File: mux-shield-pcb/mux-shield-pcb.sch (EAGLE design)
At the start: 12 parts, among them X1 BN35N61, X2 BN35N61, X3 BU-SMB-V, X4 BU-SMB-V, X5 BU-SMA-V

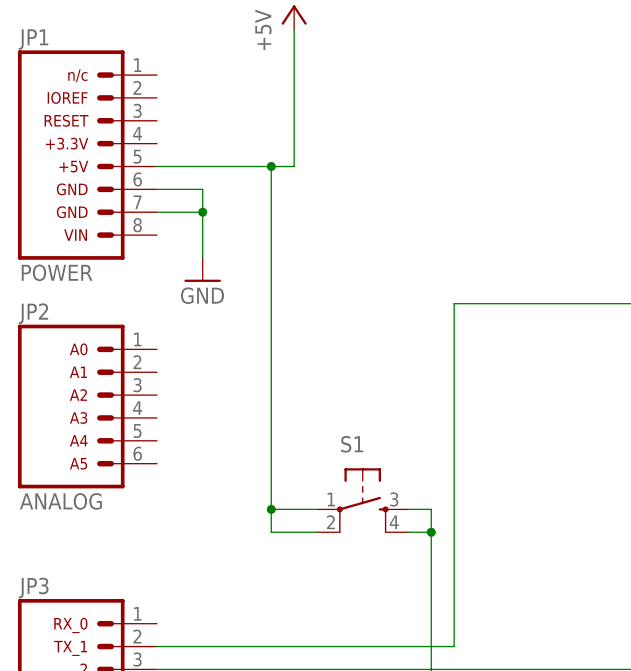
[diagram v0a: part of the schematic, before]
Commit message: Update PCB connecting button to ground rather than 5V
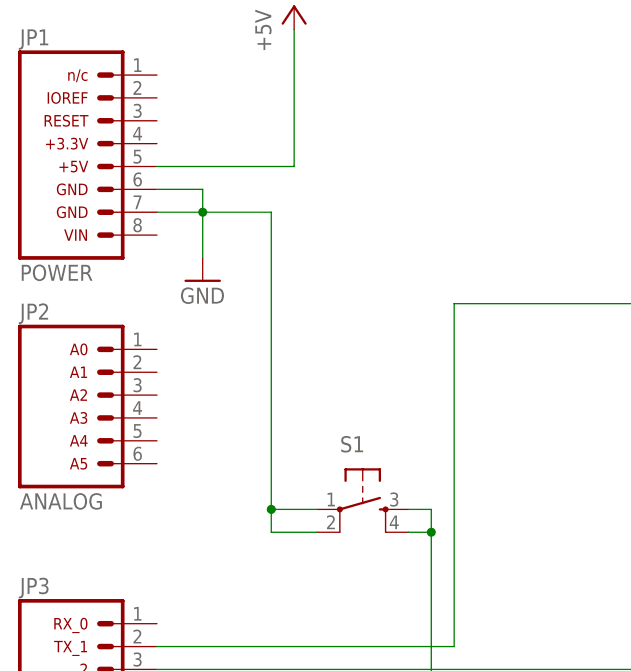
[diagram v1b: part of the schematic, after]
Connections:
- net +5V: no longer S1.1, S1.2
- net GND: now also S1.1, S1.2
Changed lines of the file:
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@@
 <wire x1="40.64" y1="177.8" x2="45.72" y2="177.8" width="0.1524" layer="91"/>
 <junction x="45.72" y="177.8"/>
+<pinref part="S1" gate="S" pin="1"/>
+<wire x1="58.42" y1="144.78" x2="53.34" y2="144.78" width="0.1524" layer="91"/>
+<pinref part="S1" gate="S" pin="2"/>
+<wire x1="58.42" y1="142.24" x2="53.34" y2="142.24" width="0.1524" layer="91"/>
+<wire x1="53.34" y1="142.24" x2="53.34" y2="144.78" width="0.1524" layer="91"/>
+<wire x1="45.72" y1="177.8" x2="53.34" y2="177.8" width="0.1524" layer="91"/>
+<wire x1="53.34" y1="177.8" x2="53.34" y2="144.78" width="0.1524" layer="91"/>
+<junction x="53.34" y="144.78"/>
 </segment>
 <segment>
@@
 <pinref part="JP1" gate="G$1" pin="5"/>
 <pinref part="P+1" gate="1" pin="+5V"/>
-<wire x1="40.64" y1="182.88" x2="53.34" y2="182.88" width="0.1524" layer="91"/>
-<wire x1="53.34" y1="182.88" x2="55.88" y2="182.88" width="0.1524" layer="91"/>
+<wire x1="40.64" y1="182.88" x2="55.88" y2="182.88" width="0.1524" layer="91"/>
 <wire x1="55.88" y1="182.88" x2="55.88" y2="198.12" width="0.1524" layer="91"/>
-<pinref part="S1" gate="S" pin="2"/>
-<wire x1="58.42" y1="142.24" x2="53.34" y2="142.24" width="0.1524" layer="91"/>
-<wire x1="53.34" y1="142.24" x2="53.34" y2="144.78" width="0.1524" layer="91"/>
-<junction x="53.34" y="182.88"/>
-<pinref part="S1" gate="S" pin="1"/>
-<wire x1="53.34" y1="144.78" x2="53.34" y2="182.88" width="0.1524" layer="91"/>
-<wire x1="58.42" y1="144.78" x2="53.34" y2="144.78" width="0.1524" layer="91"/>
-<junction x="53.34" y="144.78"/>
 </segment>
 </net>
